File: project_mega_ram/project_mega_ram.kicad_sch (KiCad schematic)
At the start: 34 parts, among them U10 74LS02, U11 74LS139, U12 CS18LV10245, U2 CS18LV10245, U4 74LS157, U5 74LS157, U6 74LS08, U7 74LS32, U8 74LS74, U9 74LS32

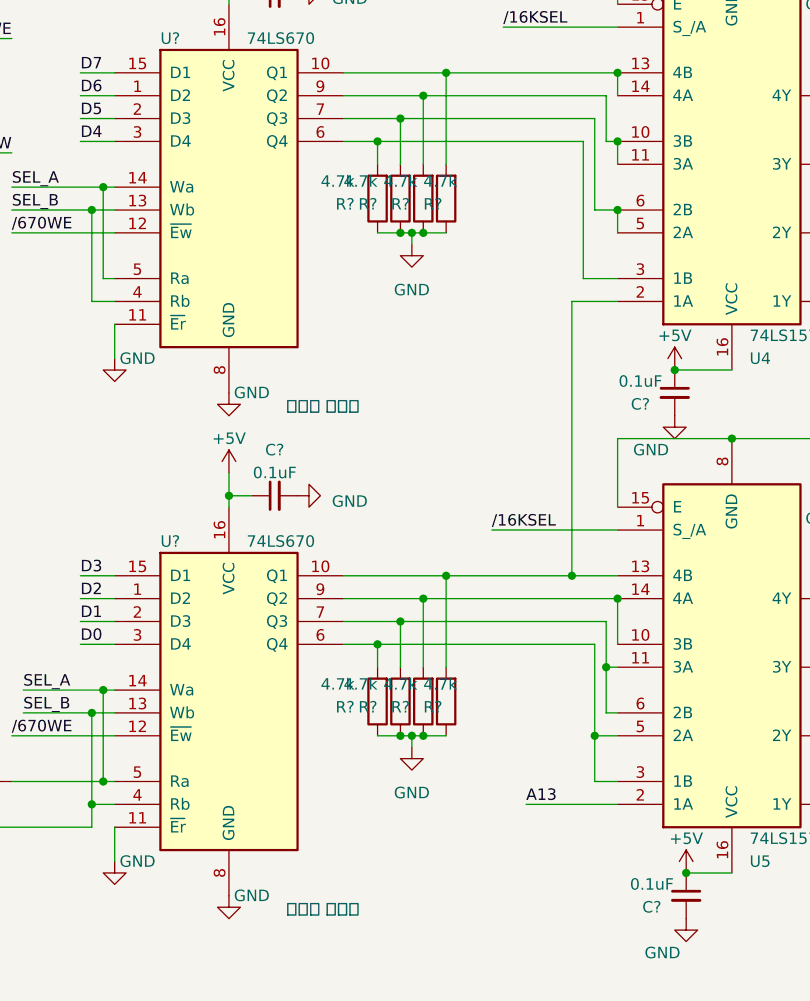
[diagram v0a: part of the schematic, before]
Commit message: Added project_mega_ram (Mega Ram Card)
Signed-off-by: ykp74 <ykp7409@gmail.com>
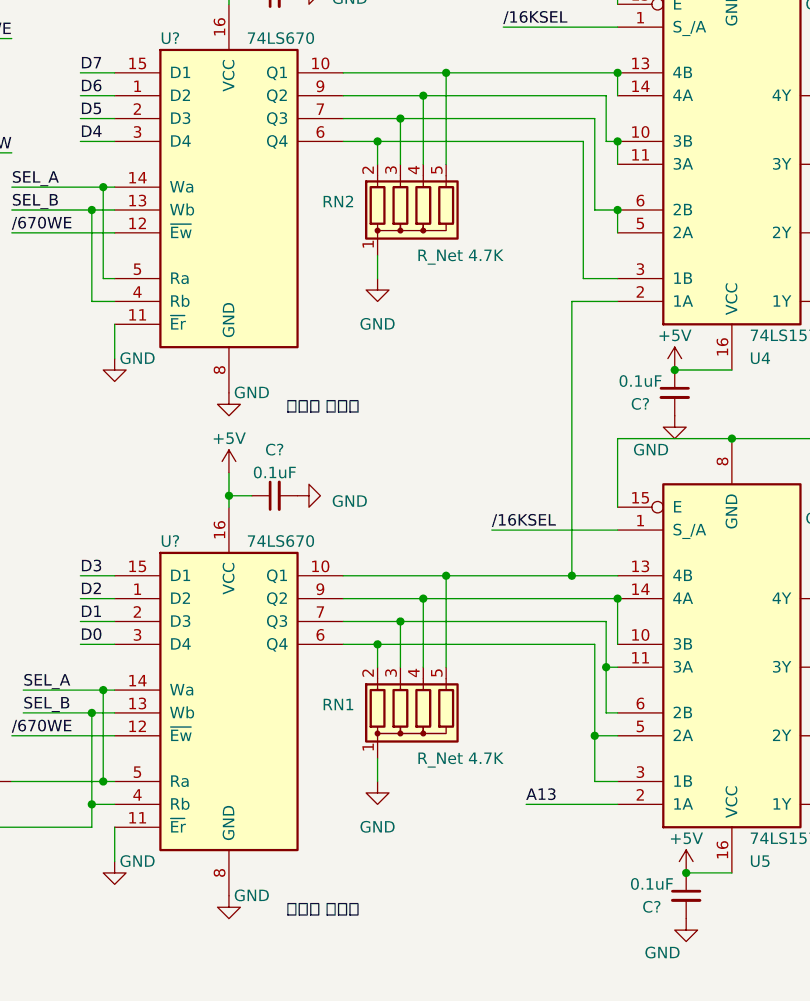
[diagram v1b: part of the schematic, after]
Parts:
- removed R? (x8): 4.7k, Resistor_THT:R_Axial_DIN0207_L6.3mm_D2.5mm_P10.16mm_Horizontal, symbol Device:R
- added RN1, RN2: R_Net 4.7K, Resistor_THT:R_Array_SIP5, symbol Device:R_Network04
- C4: footprint (none) -> Capacitor_THT:CP_Radial_D5.0mm_P2.50mm
- CE1: footprint KiCad:card_edge_connector_MSX -> Lib_add:card_edge_connector_MSX
- U10, U6, U7, U8, U9: footprint (none) -> Package_DIP:DIP-14_W7.62mm_Socket
- U11, U4, U5: footprint (none) -> Package_DIP:DIP-16_W7.62mm_Socket
- U12, U2: footprint (none) -> Package_DIP:DIP-32_W15.24mm_Socket
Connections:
- net GND: now also RN1.1 (common), RN2.1 (common)
- net at U5.10 (3B), U5.14 (4A), U?.9 (Q2): now also RN1.4 (R3)
- net at U4.2 (1A), U5.13 (4B), U?.10 (Q1): now also RN1.5 (R4)
- net at U4.3 (1B), U?.6 (Q4): now also RN2.2 (R1)
- net at U4.13 (4B), U4.14 (4A), U?.10 (Q1): now also RN2.5 (R4)
- net at U4.5 (2A), U4.6 (2B), U?.7 (Q3): now also RN2.3 (R2)
- net at U4.10 (3B), U4.11 (3A), U?.9 (Q2): now also RN2.4 (R3)
- net at U5.11 (3A), U5.6 (2B), U?.7 (Q3): now also RN1.3 (R2)
- net at U5.3 (1B), U5.5 (2A), U?.6 (Q4): now also RN1.2 (R1)

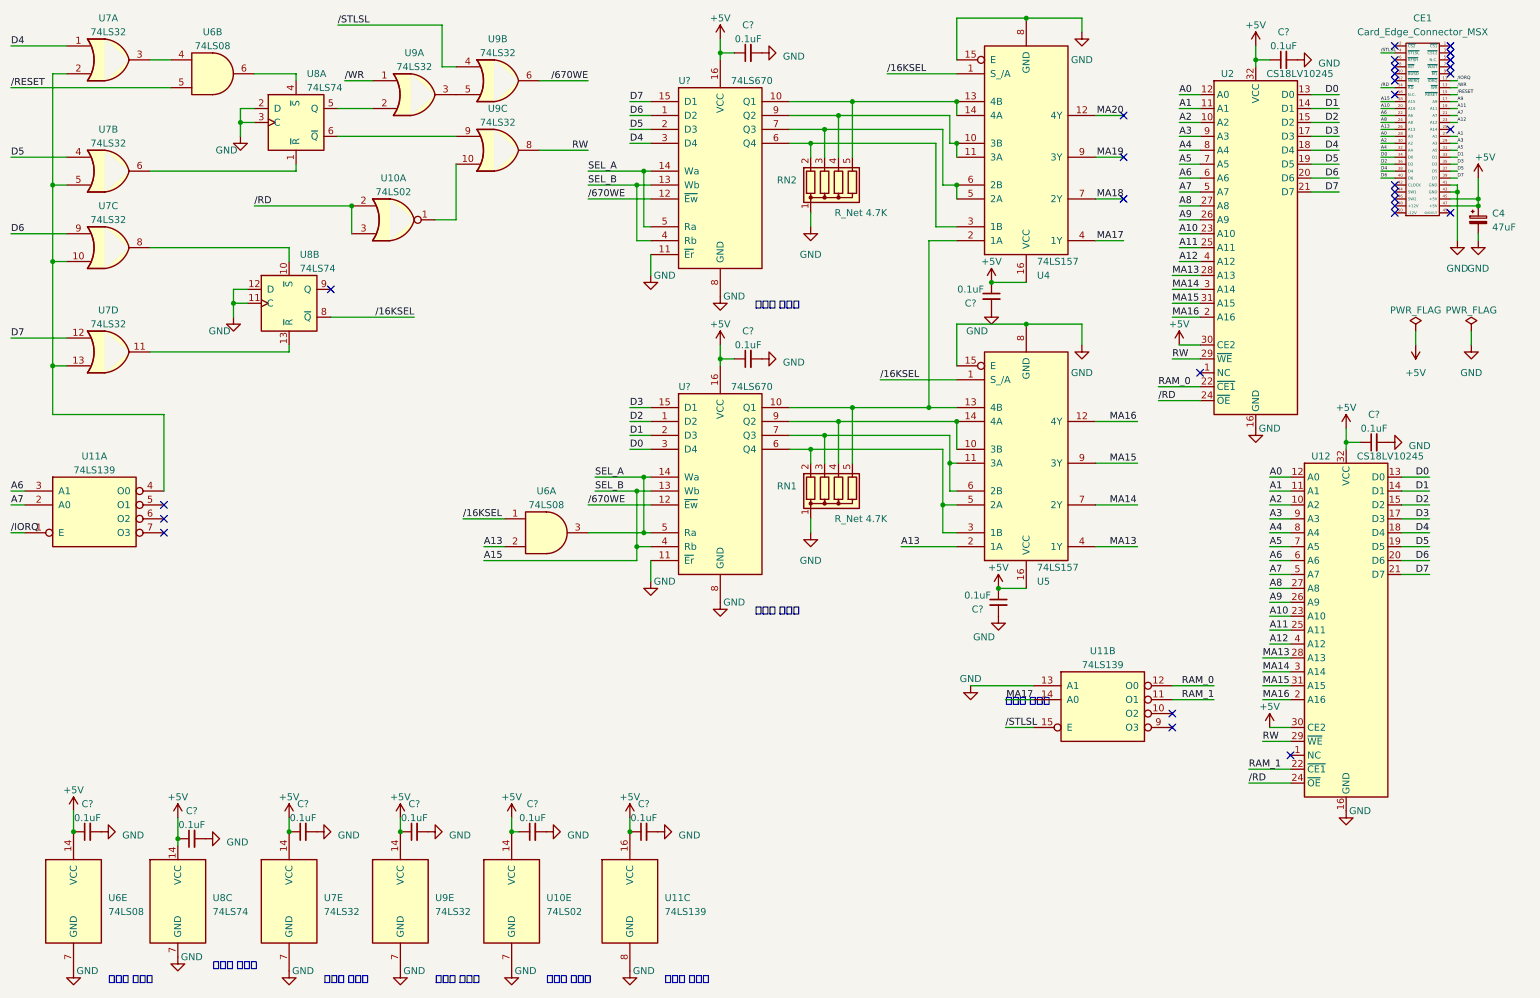
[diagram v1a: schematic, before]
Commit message: modified project_mega_ram design
Signed-off-by: Youngki Park <ykp7409@gmail.com>
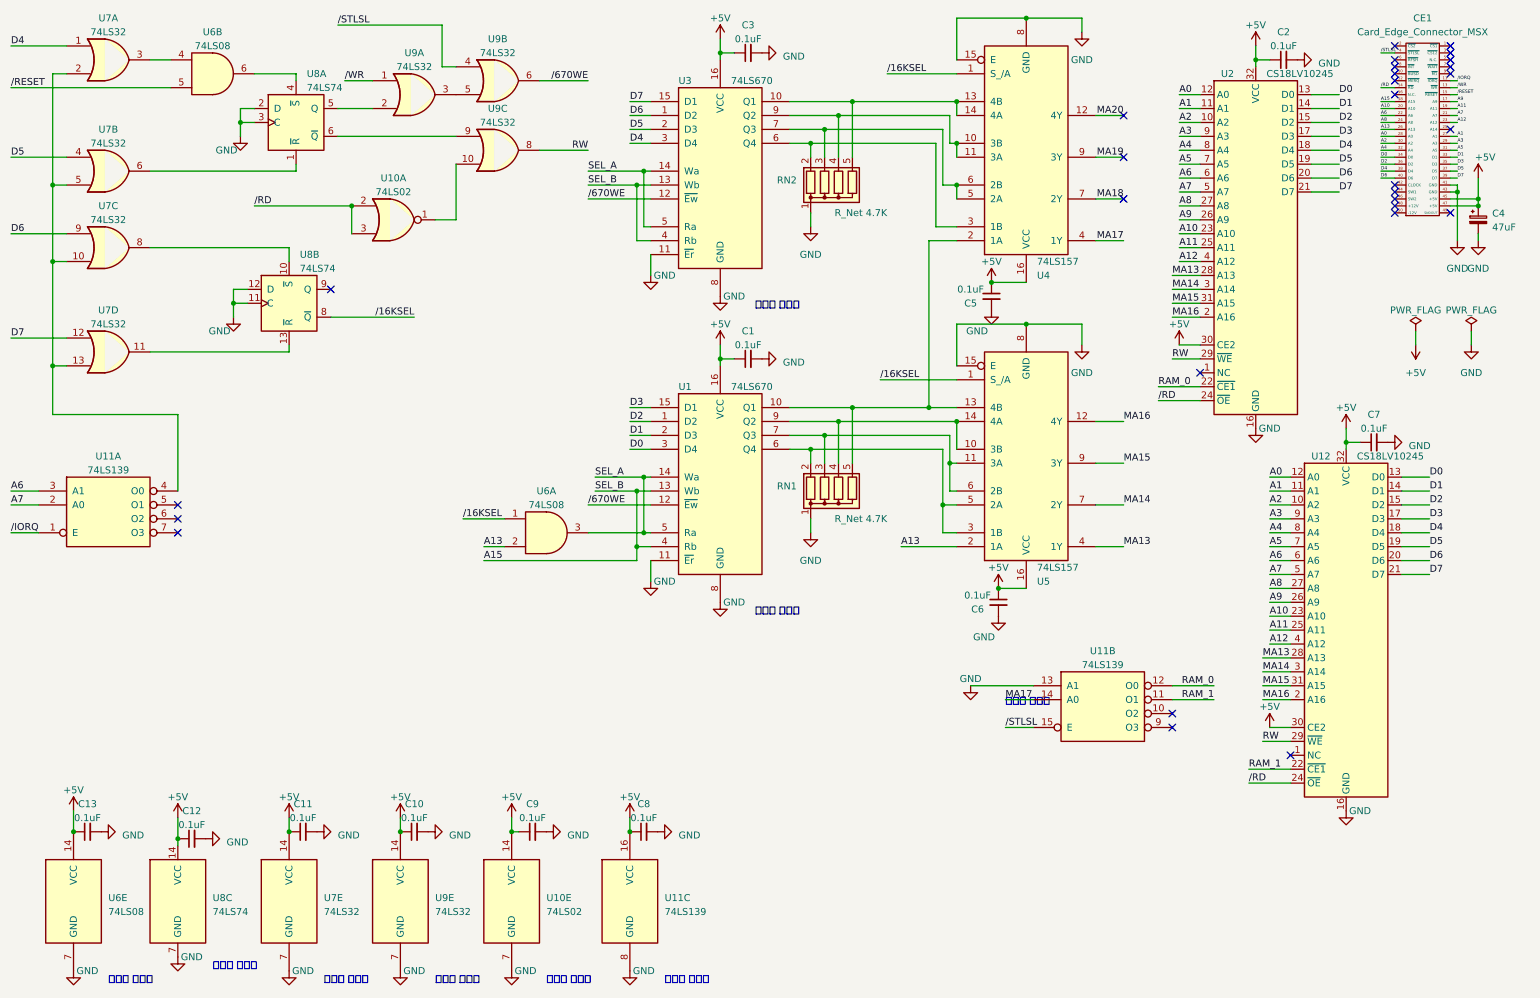
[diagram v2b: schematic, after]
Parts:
- gave numbers to parts that had none: 14
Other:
- title: (none) -> Mega Ram Pack
- moved on the sheet: U11A

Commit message: Modify Project mega ram card
Signed-off-by: Youngki Park <ykp7409@gmail.com>
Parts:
- CE1: value Card_Edge_Connector_MSX -> card_edge_connector_msx
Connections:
- net RW: no longer U12.29 (~{WE}), U2.29 (~{WE})
- net /WR: now also U12.29 (~{WE}), U2.29 (~{WE})
- no-connect marks 29 -> 30
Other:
- moved on the sheet: U10A, U11A, U6B, U7A, U7B, U7C, U7D, U8A, U8B, U9A, U9B, U9C

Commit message: modified PCB : Signed-off-by: ykp74 <ykp7409@gmail.com>
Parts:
- C4: value 47uF -> 100uF
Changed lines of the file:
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@@
 		(fields_autoplaced yes)
 		(property "Reference" "C4"
-			(at 283.21 50.8889 0)
+			(at 283.21 50.2538 0)
 			(show_name no)
 			(do_not_autoplace no)
@@
 			)
 		)
-		(property "Value" "47uF"
-			(at 283.21 53.4289 0)
+		(property "Value" "100uF"
+			(at 283.21 52.7938 0)
 			(show_name no)
 			(do_not_autoplace no)
